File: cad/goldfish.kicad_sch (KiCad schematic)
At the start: 24 parts

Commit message: Fix silkscreen on bottom edge pins
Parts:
- C1, C10, C2, C3, C4, C5: value (none) -> 0u1; footprint (none) -> Capacitor_SMD:C_0402_1005Metric
- C6: value (none) -> 4u7; footprint (none) -> Capacitor_SMD:C_0402_1005Metric
- C7, C8: value (none) -> 22p; footprint (none) -> Capacitor_SMD:C_0402_1005Metric
- C9: value (none) -> 1u; footprint (none) -> Capacitor_SMD:C_0402_1005Metric
- D1: value (none) -> D_Schottky; footprint (none) -> Diode_SMD:D_PowerDI-123
- J1: value (none) -> USB-C; footprint (none) -> usb-type-c:CX70M-24P1
- J2: value (none) -> 01x02; footprint (none) -> pins:Pins2
- J3, J4: value (none) -> 01x12; footprint (none) -> pins:Pins12
- J5: value (none) -> 01x05; footprint (none) -> pins:Pins5
- R1, R2: value (none) -> 5k1; footprint (none) -> Resistor_SMD:R_0402_1005Metric
- R3, R6: value (none) -> 10k; footprint (none) -> Resistor_SMD:R_0402_1005Metric
- R4, R5: value (none) -> 22; footprint (none) -> Resistor_SMD:R_0402_1005Metric
- U1: value (none) -> ATmega32U4; footprint (none) -> Package_DFN_QFN:QFN-44-1EP_7x7mm_P0.5mm_EP5.2x5.2mm
- X1: value (none) -> 16MHz; footprint (none) -> Crystal:Crystal_SMD_SeikoEpson_FA238-4Pin_3.2x2.5mm
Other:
- note added: "Released under the Creative Commons Attribution Share-Alike 4.0 License https://creativecommons.org/licenses/by-sa/4.0/ Original Arduino Mini Design by Team Arduino Arduino Pro Mini Design by Spark Fun Electronics Pro Micro Design by Spark Fun Electronics Goldfish Design by Lucas Jansen"
- note removed: "Released under the Creative Commons Attribution Share-Alike 4.0 License https://creativecommons.org/licenses/by-sa/4.0/ Original Arduino Mini Design by Team Arduino Arduino Pro Mini Design by Spark Fun Electronics Pro Micro Design by Spark Fun Electronics Goldfish Design by dr_derivative"

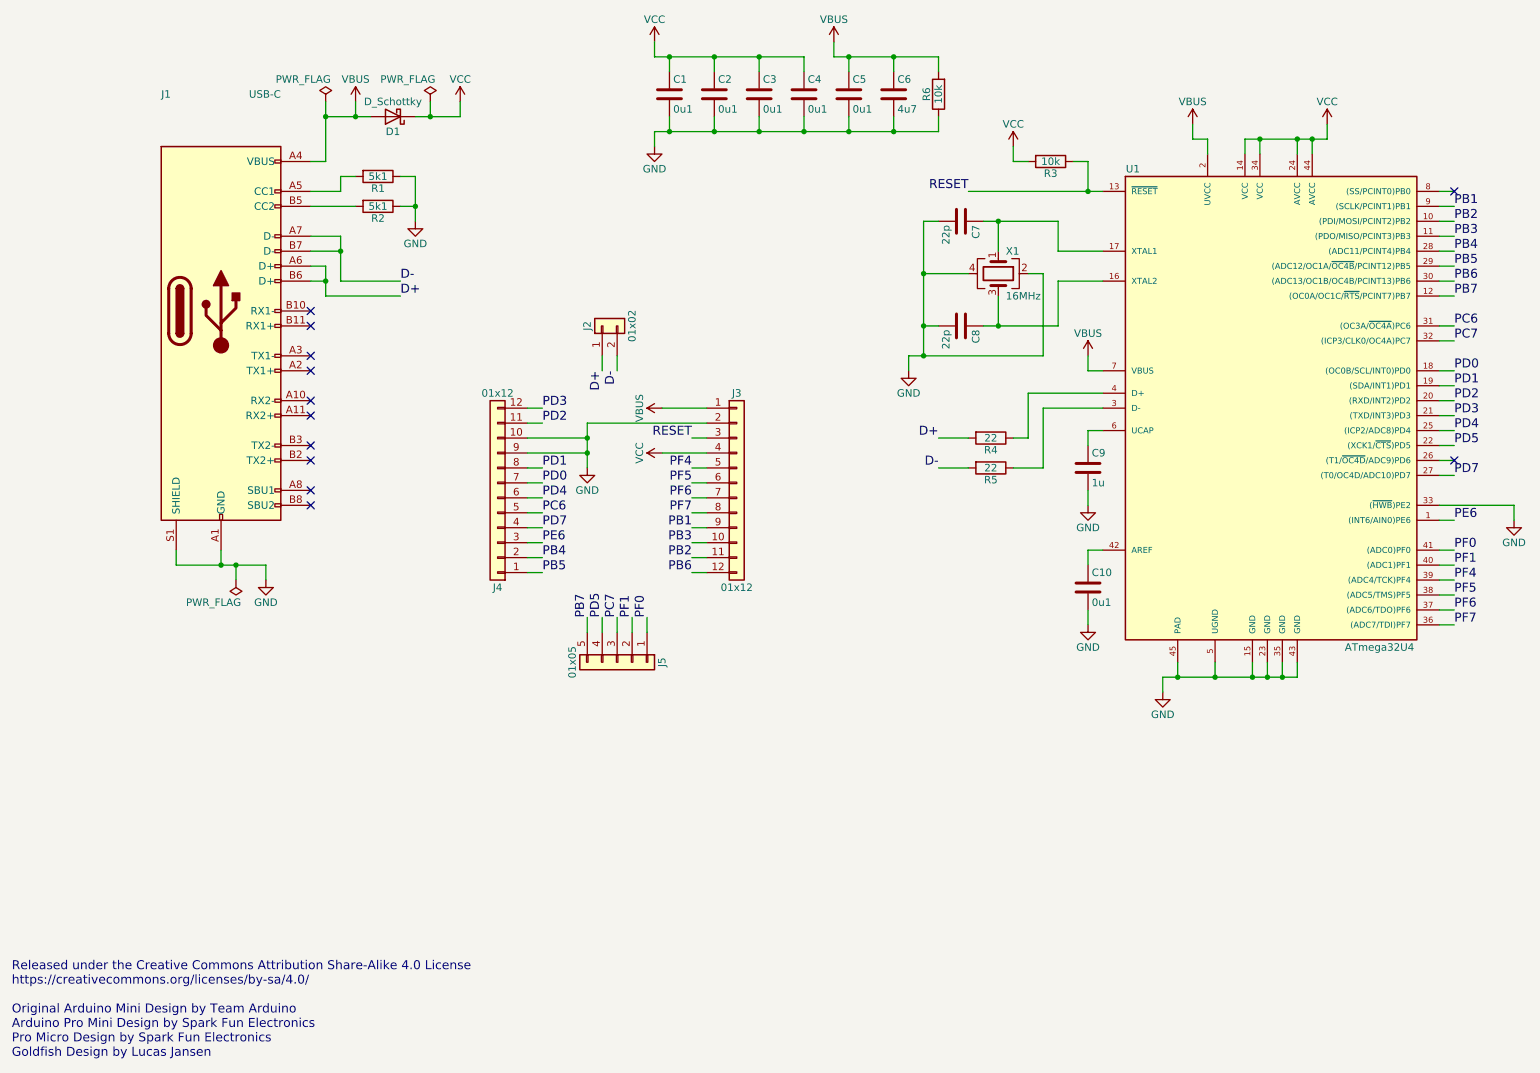
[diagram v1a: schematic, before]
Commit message: Add initial V2 design
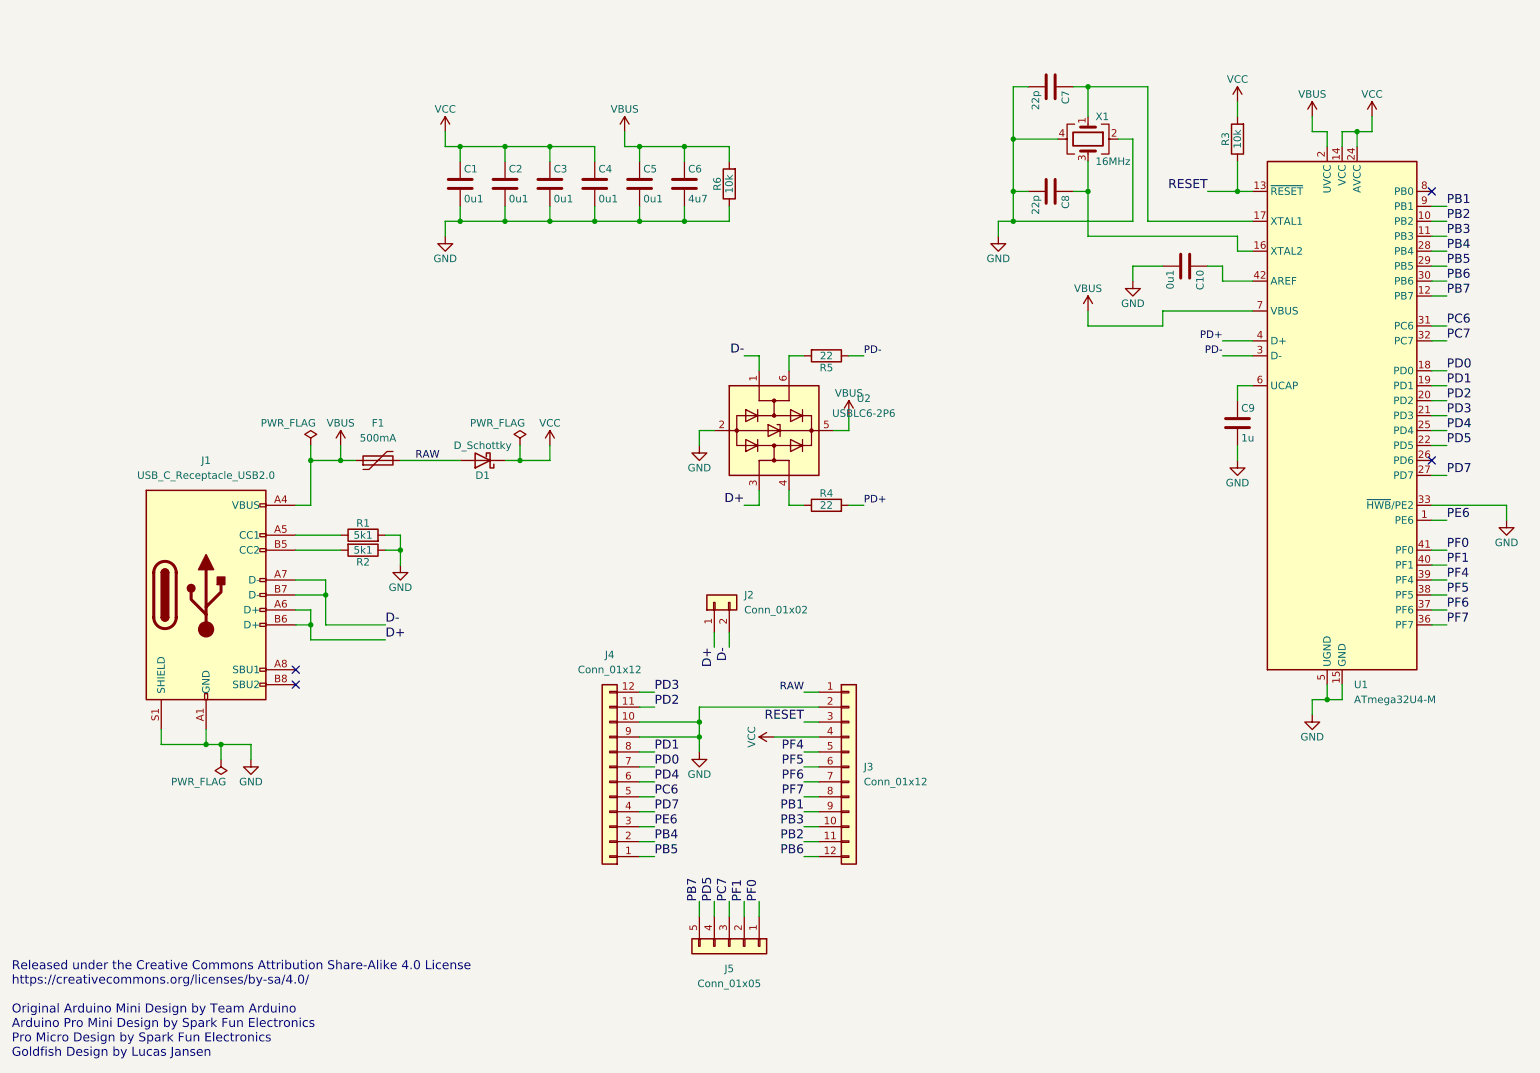
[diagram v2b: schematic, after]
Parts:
- removed J1: USB-C, usb-type-c:CX70M-24P1, symbol Connector:USB_C_Receptacle
- removed U1: ATmega32U4, Package_DFN_QFN:QFN-44-1EP_7x7mm_P0.5mm_EP5.2x5.2mm, symbol atmega32u4-ep:ATMEGA32U4-EP
- added F1: 500mA, Fuse:Fuse_0805_2012Metric, symbol Device:Polyfuse
- added J1: USB_C_Receptacle_USB2.0, Molex 216990_GCT USB45xx_HRO TYPE-C-31-M-13x:Molex-216990_GCT-USB45xx_HRO-TYPE-C-31-M-13x, symbol Connector:USB_C_Receptacle_USB2.0
- added U1: ATmega32U4-M, Package_DFN_QFN:QFN-44-1EP_7x7mm_P0.5mm_EP5.2x5.2mm, symbol MCU_Microchip_ATmega:ATmega32U4-M
- added U2: USBLC6-2P6, Package_TO_SOT_SMD:SOT-666, symbol Power_Protection:USBLC6-2P6
- C1, C10, C2, C3, C4, C5, C6, C7, C8, C9: footprint Capacitor_SMD:C_0402_1005Metric -> Capacitor_SMD:C_0603_1608Metric
- J2: value 01x02 -> Conn_01x02; footprint pins:Pins2 -> Goldfish Pins:Pins_USB
- J3, J4: value 01x12 -> Conn_01x12; footprint pins:Pins12 -> Goldfish Pins:Pins_x12_Castellated
- J5: value 01x05 -> Conn_01x05; footprint pins:Pins5 -> Goldfish Pins:Pins_x05_Castellated
- R1, R2, R3, R4, R5, R6: footprint Resistor_SMD:R_0402_1005Metric -> Resistor_SMD:R_0603_1608Metric
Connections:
- net D+: now also J1.A6 (D+), J1.B6 (D+), U2.3 (I/O2); no longer R4.2
- net D-: now also J1.A7 (D-), J1.B7 (D-), U2.1 (I/O1); no longer R5.2
- net GND: now also R1.2, J1.A1 (GND), J1.A12 (GND), J1.B1 (GND), J1.B12 (GND), J1.S1 (SHIELD), U1.15 (GND), U1.23 (GND), U1.33 (~{HWB}/PE2), U1.35 (GND), U1.43 (GND), U1.45 (GND), U1.5 (UGND), U2.2 (GND); no longer R1.1
- net PB1: now also U1.9 (PB1)
- net PB2: now also U1.10 (PB2)
- net PB3: now also U1.11 (PB3)
- net PB4: now also U1.28 (PB4)
- net PB5: now also U1.29 (PB5)
- net PB6: now also U1.30 (PB6)
- net PB7: now also U1.12 (PB7)
- net PC6: now also U1.31 (PC6)
- net PC7: now also U1.32 (PC7)
- net PD0: now also U1.18 (PD0)
- net PD1: now also U1.19 (PD1)
- net PD2: now also U1.20 (PD2)
- net PD3: now also U1.21 (PD3)
- net PD4: now also U1.25 (PD4)
- net PD5: now also U1.22 (PD5)
- net PD7: now also U1.27 (PD7)
- net PE6: now also U1.1 (PE6)
- net PF0: now also U1.41 (PF0)
- net PF1: now also U1.40 (PF1)
- net PF4: now also U1.39 (PF4)
- net PF5: now also U1.38 (PF5)
- net PF6: now also U1.37 (PF6)
- net PF7: now also U1.36 (PF7)
- net RESET: now also U1.13 (~{RESET})
- net VBUS: now also F1.1, J1.A4 (VBUS), J1.A9 (VBUS), J1.B4 (VBUS), J1.B9 (VBUS), U1.2 (UVCC), U1.7 (VBUS), U2.5 (VBUS); no longer D1.2 (A), J3.1 (Pin_1)
- net VCC: now also U1.14 (VCC), U1.24 (AVCC), U1.34 (VCC), U1.44 (AVCC)
- net at R2.2: now also J1.B5 (CC2)
- net at R4.1: now also U2.4 (I/O2)
- net PD-: now reaches R5.1
- net PD-: now also U1.3 (D-)
- net at C8.1, X1.3: now also U1.16 (XTAL2)
- net at C7.1, X1.1: now also U1.17 (XTAL1)
- net at C10.1: now also U1.42 (AREF)
- net at C9.1: now also U1.6 (UCAP)
- new net: J1.A5 (CC1), R1.1
- new net: R5.2, U2.6 (I/O1)
- new net PD+: R4.2, U1.4 (D+)
- new net RAW: D1.2 (A), F1.2, J3.1 (Pin_1)
- no-connect marks 12 -> 4
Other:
- title: Goldfish -> Goldfish v2

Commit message: Switch D1 to SOD 123F
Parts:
- D1: footprint Diode_SMD:D_PowerDI-123 -> Diode_SMD:D_SOD-123F
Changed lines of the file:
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@@
     (property "Reference" "D1" (id 0) (at 97.79 93.98 0))
     (property "Value" "D_Schottky" (id 1) (at 97.79 88.9 0))
-    (property "Footprint" "Diode_SMD:D_PowerDI-123" (id 2) (at 97.79 91.44 0)
+    (property "Footprint" "Diode_SMD:D_SOD-123F" (id 2) (at 97.79 91.44 0)
       (effects (font (size 1.27 1.27)) hide)
     )
@@
     )
     (path "/be61cf1a-4f09-4ef2-92bc-b6ed5020a3ac"
-      (reference "D1") (unit 1) (value "D_Schottky") (footprint "Diode_SMD:D_PowerDI-123")
+      (reference "D1") (unit 1) (value "D_Schottky") (footprint "Diode_SMD:D_SOD-123F")
     )
     (path "/c6672b65-6043-42b5-a2d1-8a8e4648a917"
